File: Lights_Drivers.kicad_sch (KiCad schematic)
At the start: 15 parts, among them Q3 2N7002, Q4 2N7002, Q7 2N7002, U23 SI8261ABC-IS, U24 SI8261ABC-IS, U6 SI8261ABC-IS

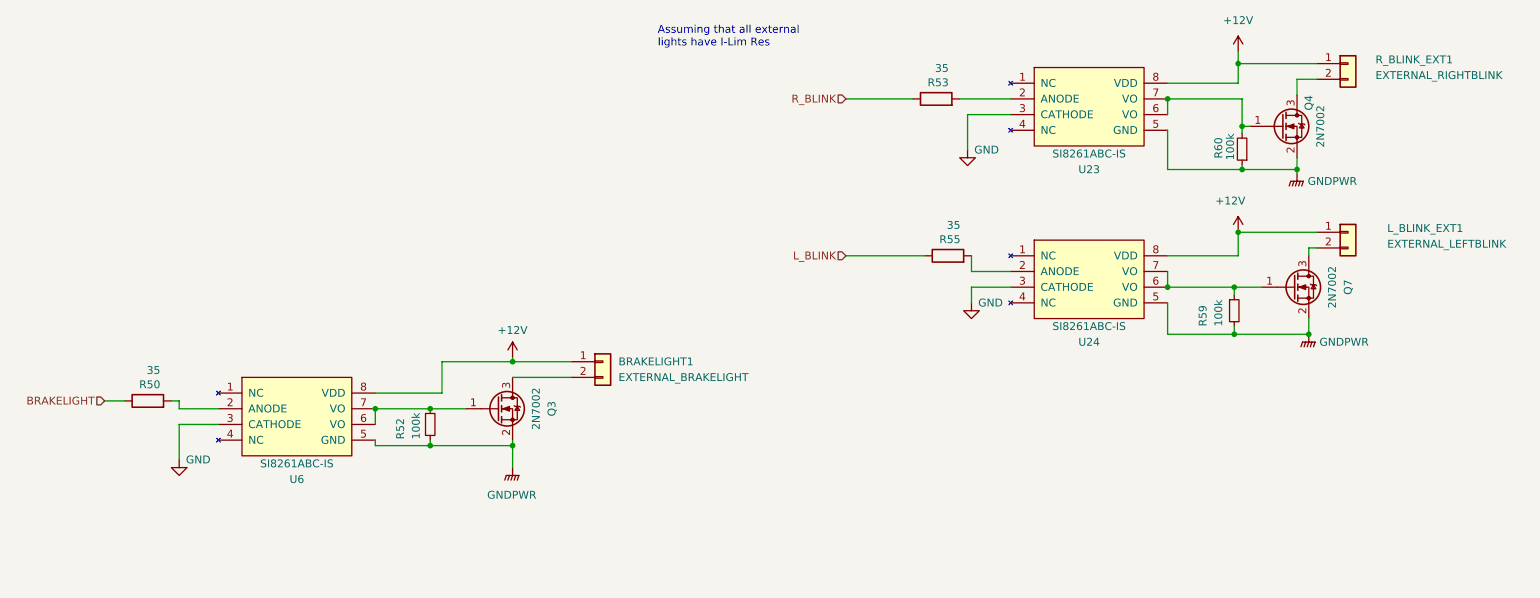
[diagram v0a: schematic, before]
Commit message: Flipped optoisolators, changed resistor values, added second connector to motor can and disconnected shield pins for now since I haven't seen them used (will chack against old version to see what the circuit looked like), copied power-in circuit from contactor board, added optoisolator to timer and blinker light connection.
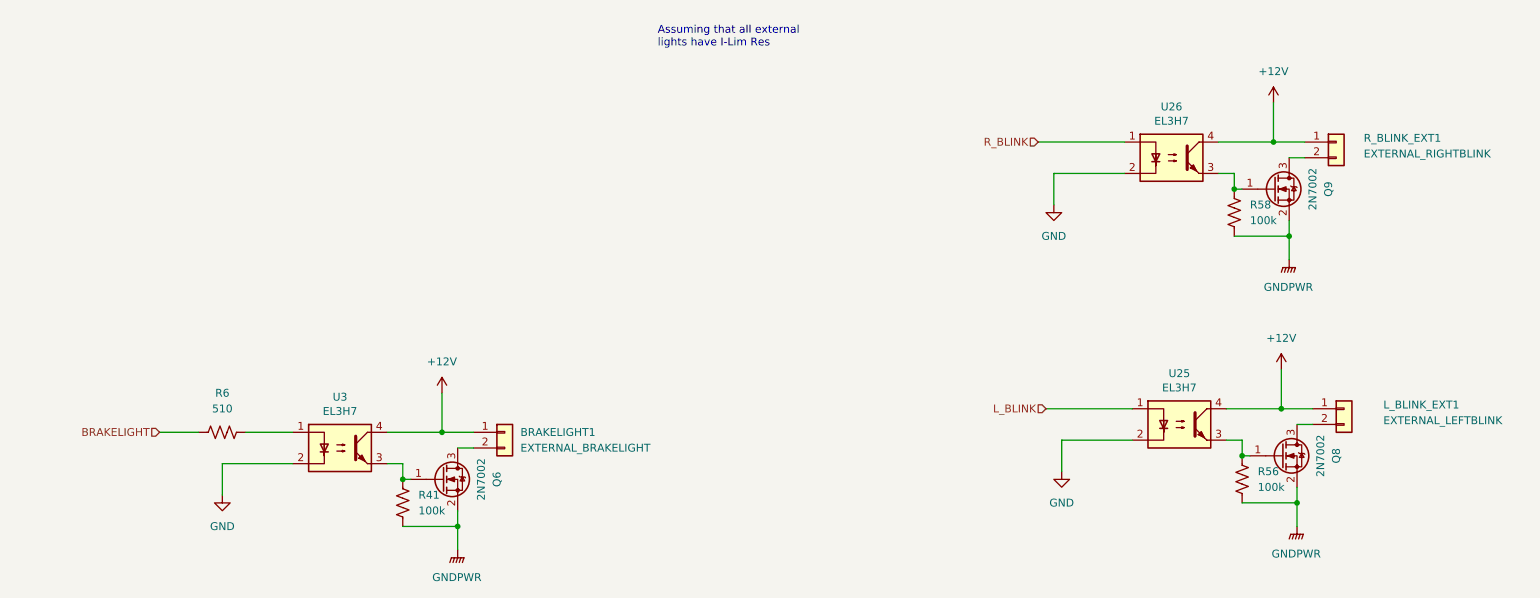
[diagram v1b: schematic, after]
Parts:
- removed Q3, Q4, Q7: 2N7002, Package_TO_SOT_SMD:SOT-23, symbol Transistor_FET:2N7002
- removed R50, R53, R55: 35, Resistor_SMD:R_0805_2012Metric, symbol Device:R
- removed R52, R59, R60: 100k, Resistor_SMD:R_0805_2012Metric, symbol Device:R_Small
- removed U23, U24, U6: SI8261ABC-IS, Package_SO:SOIC-8_3.9x4.9mm_P1.27mm, symbol utsvt-bps:SI8261ABC-IS
- added Q6, Q8, Q9: 2N7002, Package_TO_SOT_SMD:SOT-23, symbol Transistor_FET:2N7002
- added R41, R56, R58: 100k, Resistor_SMD:R_0805_2012Metric, symbol Device:R_US
- added R6: 510, symbol Device:R_US
- added U25, U26, U3: EL3H7, Package_DIP:DIP-4_W7.62mm, symbol Isolator:SFH617A-1
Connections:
- net +12V: now also U25.4, U26.4, U3.4
- net BRAKELIGHT: now also R6.1
- net GND: now also U25.2, U26.2, U3.2
- net GNDPWR: now also Q6.2 (S), Q8.2 (S), Q9.2 (S), R41.2, R56.2, R58.2
- net L_BLINK: now also U25.1
- net R_BLINK: now also U26.1
- net at L_BLINK_EXT1.2 (Pin_2): now also Q8.3 (D)
- net at R_BLINK_EXT1.2 (Pin_2): now also Q9.3 (D)
- net at BRAKELIGHT1.2 (Pin_2): now also Q6.3 (D)
- new net: Q8.1 (G), R56.1, U25.3
- new net: Q9.1 (G), R58.1, U26.3
- new net: Q6.1 (G), R41.1, U3.3
- new net: R6.2, U3.1
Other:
- moved on the sheet: BRAKELIGHT1, L_BLINK_EXT1, R_BLINK_EXT1

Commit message: Added footprints. I think this is everything except the fuse.
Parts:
- R6: footprint (none) -> Resistor_SMD:R_0805_2012Metric
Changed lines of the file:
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@@
 			)
 		)
-		(property "Footprint" ""
+		(property "Footprint" "Resistor_SMD:R_0805_2012Metric"
 			(at 53.594 104.394 90)
 			(effects

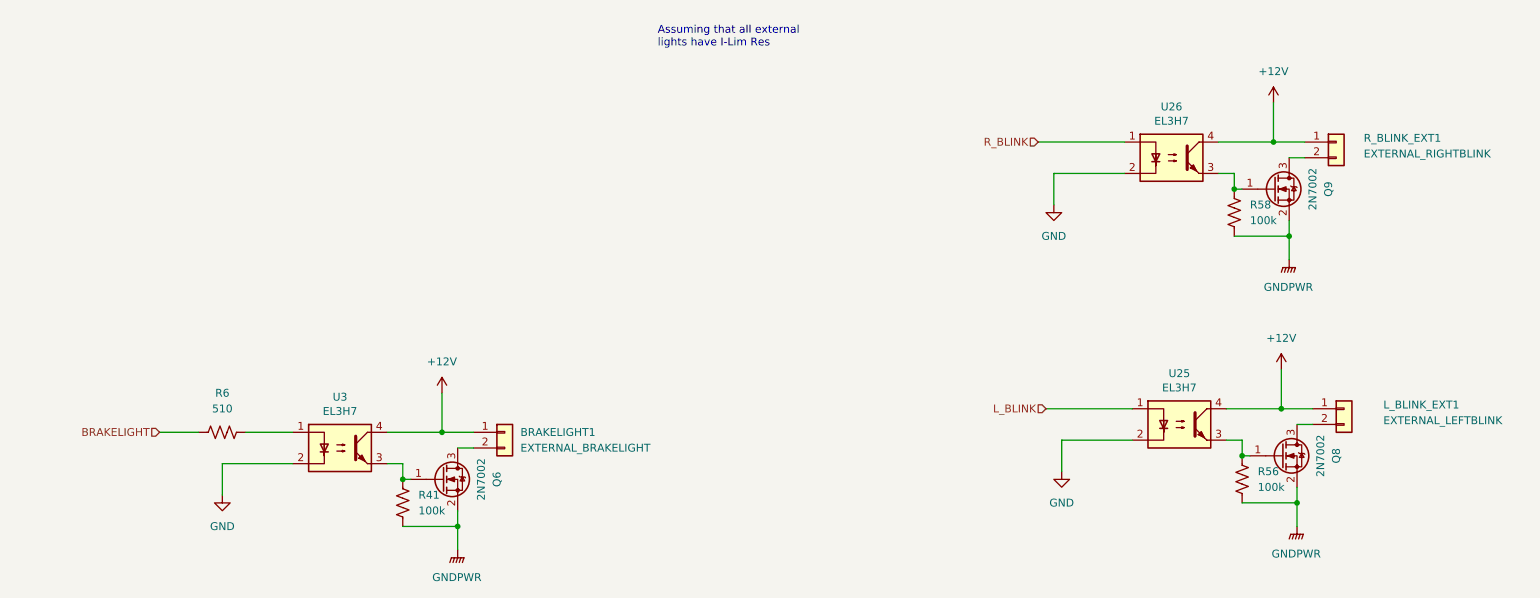
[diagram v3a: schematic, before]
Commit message: renamed power state indicators to contactors and removed unused contactors, added current limiting resistors to lights drivers, changed mosfet to new mosfet
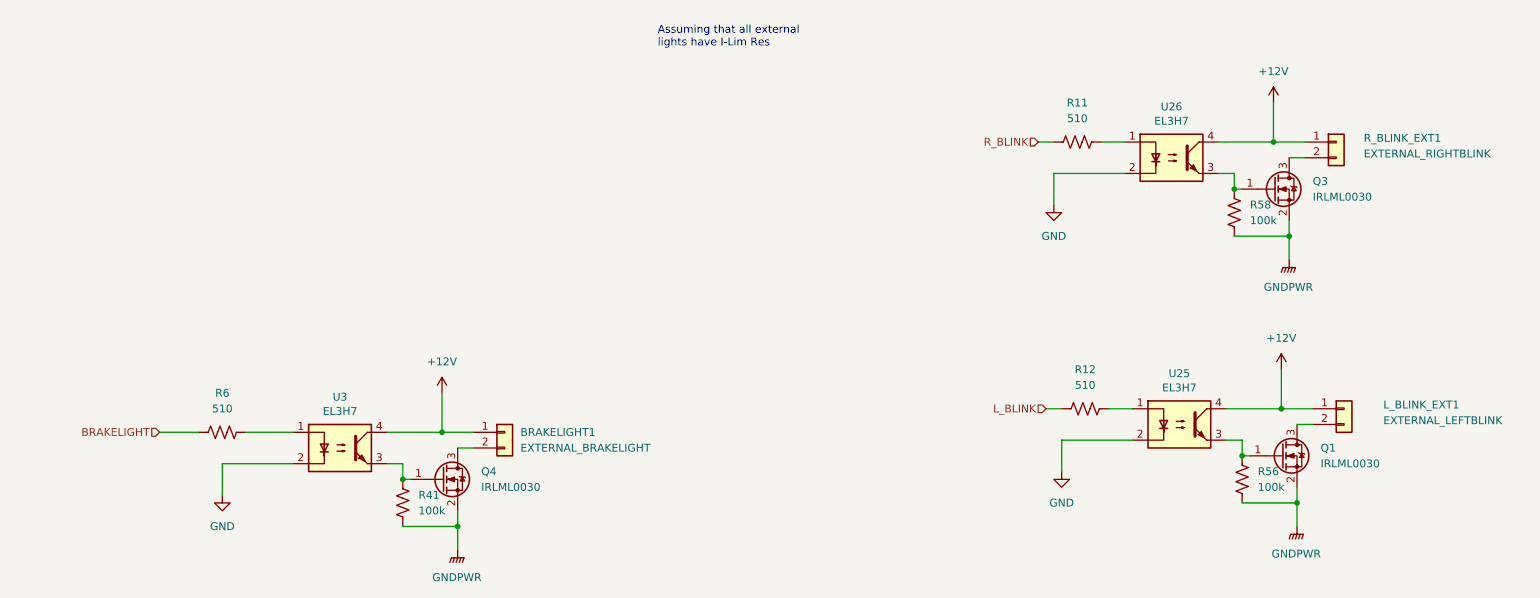
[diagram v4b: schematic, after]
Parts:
- removed Q6, Q8, Q9: 2N7002, Package_TO_SOT_SMD:SOT-23, symbol Transistor_FET:2N7002
- added Q1, Q3, Q4: IRLML0030, Package_TO_SOT_SMD:SOT-23, symbol Transistor_FET:IRLML0030
- added R11, R12: 510, symbol Device:R_US
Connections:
- net GNDPWR: now also Q1.2 (S), Q3.2 (S), Q4.2 (S)
- net L_BLINK: now also R12.1; no longer U25.1
- net R_BLINK: now also R11.1; no longer U26.1
- net at R56.1, U25.3: now also Q1.1 (G)
- net at L_BLINK_EXT1.2 (Pin_2): now also Q1.3 (D)
- net at R58.1, U26.3: now also Q3.1 (G)
- net at R_BLINK_EXT1.2 (Pin_2): now also Q3.3 (D)
- net at R41.1, U3.3: now also Q4.1 (G)
- net at BRAKELIGHT1.2 (Pin_2): now also Q4.3 (D)
- new net: R12.2, U25.1
- new net: R11.2, U26.1

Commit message: fixed some footprints and part numbers
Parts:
- Q1, Q3, Q4: Mouser Part Number (none) -> 771-BUK9M23-80EX
- R11, R12: footprint (none) -> Resistor_SMD:R_0805_2012Metric; Mouser Part Number (none) -> 71-CRCW0805510RFKEAC
- R41, R56, R58: Mouser Part Number (none) -> 71-CRCW0805100KFKEAC
- R6: Mouser Part Number (none) -> 71-CRCW0805510RFKEAC
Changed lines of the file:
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@@
 			)
 		)
-		(property "Footprint" ""
+		(property "Footprint" "Resistor_SMD:R_0805_2012Metric"
 			(at 192.024 57.404 90)
 			(effects
@@
 		)
 		(property "Vds" ""
+			(at 191.77 58.42 0)
+			(effects
+				(font
+					(size 1.27 1.27)
+				)
+				(hide yes)
+			)
+		)
+		(property "Mouser Part Number" "71-CRCW0805510RFKEAC"
 			(at 191.77 58.42 0)
 			(effects
@@
 			)
 		)
+		(property "Mouser Part Number" "771-BUK9M23-80EX"
+			(at 224.79 109.22 0)
+			(effects
+				(font
+					(size 1.27 1.27)
+				)
+				(hide yes)
+			)
+		)
 		(pin "2"
 		)
@@
 			)
 		)
+		(property "Mouser Part Number" "771-BUK9M23-80EX"
+			(at 223.52 66.04 0)
+			(effects
+				(font
+					(size 1.27 1.27)
+				)
+				(hide yes)
+			)
+		)
 		(pin "2"
 		)
@@
 			)
 		)
-		(property "Footprint" ""
+		(property "Footprint" "Resistor_SMD:R_0805_2012Metric"
 			(at 193.294 100.584 90)
 			(effects
@@
 		)
 		(property "Vds" ""
+			(at 193.04 101.6 0)
+			(effects
+				(font
+					(size 1.27 1.27)
+				)
+				(hide yes)
+			)
+		)
+		(property "Mouser Part Number" "71-CRCW0805510RFKEAC"
 			(at 193.04 101.6 0)
 			(effects
@@
 			)
 		)
+		(property "Mouser Part Number" "71-CRCW0805100KFKEAC"
+			(at 82.55 116.84 0)
+			(effects
+				(font
+					(size 1.27 1.27)
+				)
+				(hide yes)
+			)
+		)
 		(pin "2"
 		)
@@
 			)
 		)
+		(property "Mouser Part Number" "771-BUK9M23-80EX"
+			(at 88.9 113.03 0)
+			(effects
+				(font
+					(size 1.27 1.27)
+				)
+				(hide yes)
+			)
+		)
 		(pin "2"
 		)
@@
 			)
 		)
+		(property "Mouser Part Number" "71-CRCW0805100KFKEAC"
+			(at 218.44 113.03 0)
+			(effects
+				(font
+					(size 1.27 1.27)
+				)
+				(hide yes)
+			)
+		)
 		(pin "2"
 		)
@@
 			)
 		)
+		(property "Mouser Part Number" "71-CRCW0805510RFKEAC"
+			(at 53.34 105.41 0)
+			(effects
+				(font
+					(size 1.27 1.27)
+				)
+				(hide yes)
+			)
+		)
 		(pin "2"
 		)
@@
 			(at 217.17 69.85 0)
 			(effects
+				(font
+					(size 1.27 1.27)
+				)
+				(hide yes)
+			)
+		)
+		(property "Mouser Part Number" "71-CRCW0805100KFKEAC"
+			(at 217.17 69.85 0)
+			(effects

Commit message: Added/checked datasheet links/part numbers, deleted accel_pot2 and brake_pot2 hierarchical labels and changed corresponding pins (PC2, PC3) to GPIO on the now-2x5 extra GPIO connector.
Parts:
- Q1, Q3, Q4: Mouser Part Number 771-BUK9M23-80EX -> (none); P/N (none) -> IRLML0030TRPBF
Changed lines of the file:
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@@
 			)
 		)
-		(property "Datasheet" "https://everlightamericas.com/index.php?controller=attachment&id_attachment=2584"
+		(property "Datasheet" "https://www.mouser.com/ProductDetail/Everlight/EL3H7DTA-VG?qs=8PzhAHr7IdO5ivSzPAFioA%3D%3D&utm_id=21629221803&gad_source=1&gclid=Cj0KCQiArby5BhCDARIsAIJvjIRxO0jcjcKfnV1hER0ZGDMF9W_FecGmdKXwVqQCsmJYIZvEtRfuUkAaAnFwEALw_wcB"
 			(at 208.28 104.14 0)
 			(effects
@@
 			)
 		)
-		(property "Datasheet" "~"
+		(property "Datasheet" "https://www.mouser.in/ProductDetail/Vishay-Dale/CRCW0805510RFKEAC?qs=E3Y5ESvWgWP%252BBvcXzqF1aQ%3D%3D"
 			(at 191.77 58.42 0)
 			(effects
@@
 			)
 		)
-		(property "Mouser Part Number" "771-BUK9M23-80EX"
+		(property "Mouser Part Number" ""
+			(at 224.79 109.22 0)
+			(effects
+				(font
+					(size 1.27 1.27)
+				)
+				(hide yes)
+			)
+		)
+		(property "P/N" "  IRLML0030TRPBF"
 			(at 224.79 109.22 0)
 			(effects
@@
 			)
 		)
-		(property "Datasheet" "https://everlightamericas.com/index.php?controller=attachment&id_attachment=2584"
+		(property "Datasheet" "https://www.mouser.com/ProductDetail/Everlight/EL3H7DTA-VG?qs=8PzhAHr7IdO5ivSzPAFioA%3D%3D&utm_id=21629221803&gad_source=1&gclid=Cj0KCQiArby5BhCDARIsAIJvjIRxO0jcjcKfnV1hER0ZGDMF9W_FecGmdKXwVqQCsmJYIZvEtRfuUkAaAnFwEALw_wcB"
 			(at 72.39 107.95 0)
 			(effects
@@
 			)
 		)
-		(property "Mouser Part Number" "771-BUK9M23-80EX"
+		(property "Mouser Part Number" ""
+			(at 223.52 66.04 0)
+			(effects
+				(font
+					(size 1.27 1.27)
+				)
+				(hide yes)
+			)
+		)
+		(property "P/N" "  IRLML0030TRPBF"
 			(at 223.52 66.04 0)
 			(effects
@@
 			)
 		)
-		(property "Datasheet" "~"
+		(property "Datasheet" "https://www.mouser.in/ProductDetail/Vishay-Dale/CRCW0805510RFKEAC?qs=E3Y5ESvWgWP%252BBvcXzqF1aQ%3D%3D"
 			(at 193.04 101.6 0)
 			(effects
@@
 			)
 		)
-		(property "Datasheet" "~"
+		(property "Datasheet" "https://www.mouser.in/ProductDetail/Vishay-Dale/CRCW0805100KFKEAC?qs=E3Y5ESvWgWORJvbAiaO1ug%3D%3D"
 			(at 82.55 116.84 0)
 			(effects
@@
 			)
 		)
-		(property "Datasheet" "https://everlightamericas.com/index.php?controller=attachment&id_attachment=2584"
+		(property "Datasheet" "https://www.mouser.com/ProductDetail/Everlight/EL3H7DTA-VG?qs=8PzhAHr7IdO5ivSzPAFioA%3D%3D&utm_id=21629221803&gad_source=1&gclid=Cj0KCQiArby5BhCDARIsAIJvjIRxO0jcjcKfnV1hER0ZGDMF9W_FecGmdKXwVqQCsmJYIZvEtRfuUkAaAnFwEALw_wcB"
 			(at 207.01 60.96 0)
 			(effects
@@
 			)
 		)
-		(property "Mouser Part Number" "771-BUK9M23-80EX"
+		(property "Mouser Part Number" ""
+			(at 88.9 113.03 0)
+			(effects
+				(font
+					(size 1.27 1.27)
+				)
+				(hide yes)
+			)
+		)
+		(property "P/N" "  IRLML0030TRPBF"
 			(at 88.9 113.03 0)
 			(effects
@@
 			)
 		)
-		(property "Datasheet" "~"
+		(property "Datasheet" "https://www.mouser.in/ProductDetail/Vishay-Dale/CRCW0805100KFKEAC?qs=E3Y5ESvWgWORJvbAiaO1ug%3D%3D"
 			(at 218.44 113.03 0)
 			(effects
@@
 			)
 		)
-		(property "Datasheet" "~"
+		(property "Datasheet" "https://www.mouser.in/ProductDetail/Vishay-Dale/CRCW0805510RFKEAC?qs=E3Y5ESvWgWP%252BBvcXzqF1aQ%3D%3D"
 			(at 53.34 105.41 0)
 			(effects
@@
 			)
 		)
-		(property "Datasheet" "~"
+		(property "Datasheet" "https://www.mouser.in/ProductDetail/Vishay-Dale/CRCW0805100KFKEAC?qs=E3Y5ESvWgWORJvbAiaO1ug%3D%3D"
 			(at 217.17 69.85 0)
 			(effects

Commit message: Changed EL3H7 footprint from through-hole to SMD.
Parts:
- U25, U26, U3: footprint Package_DIP:DIP-4_W7.62mm -> Package_SO:SSOP-4_4.4x2.6mm_P1.27mm
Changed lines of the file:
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@@
 			)
 		)
-		(property "Footprint" "Package_DIP:DIP-4_W7.62mm"
+		(property "Footprint" "Package_SO:SSOP-4_4.4x2.6mm_P1.27mm"
 			(at 203.2 109.22 0)
 			(effects
@@
 			)
 		)
-		(property "Footprint" "Package_DIP:DIP-4_W7.62mm"
+		(property "Footprint" "Package_SO:SSOP-4_4.4x2.6mm_P1.27mm"
 			(at 67.31 113.03 0)
 			(effects
@@
 			)
 		)
-		(property "Footprint" "Package_DIP:DIP-4_W7.62mm"
+		(property "Footprint" "Package_SO:SSOP-4_4.4x2.6mm_P1.27mm"
 			(at 201.93 66.04 0)
 			(effects

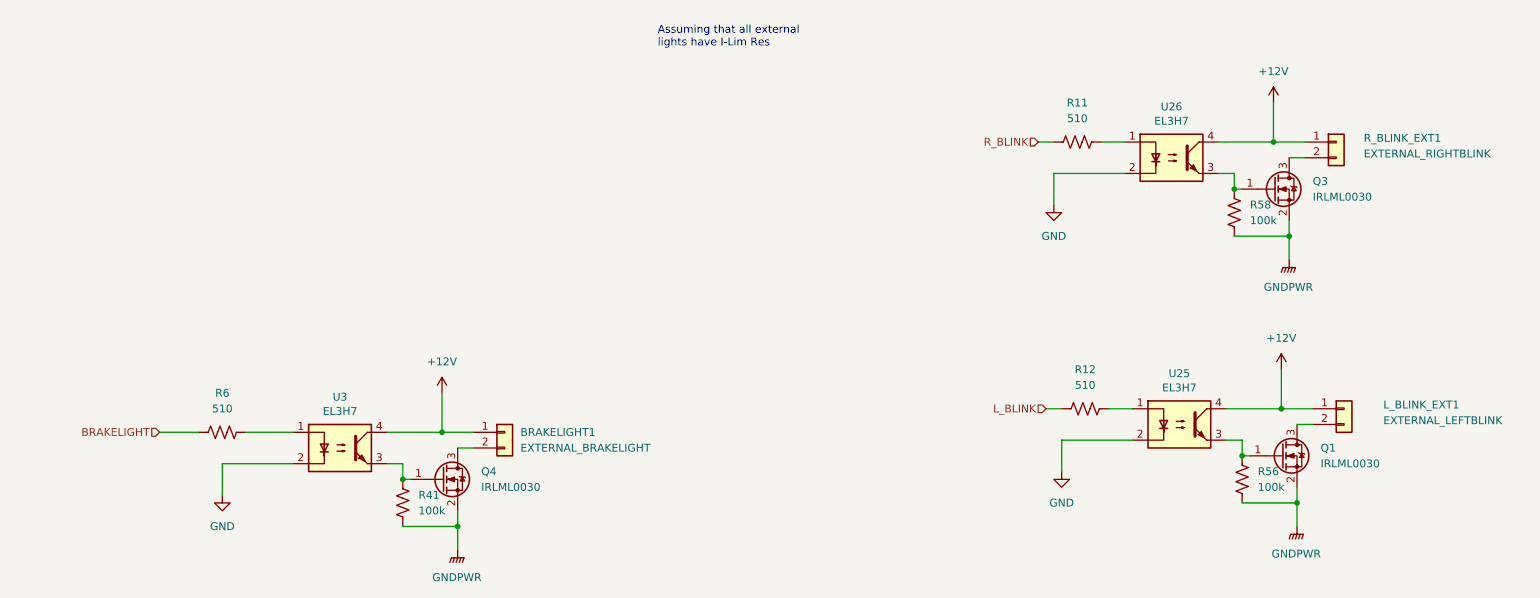
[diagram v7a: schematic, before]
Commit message: Added 3A fuse to lights (estimated 9 lights, ~1.8 A plus buffer, changed fuse datasheet to match part number.
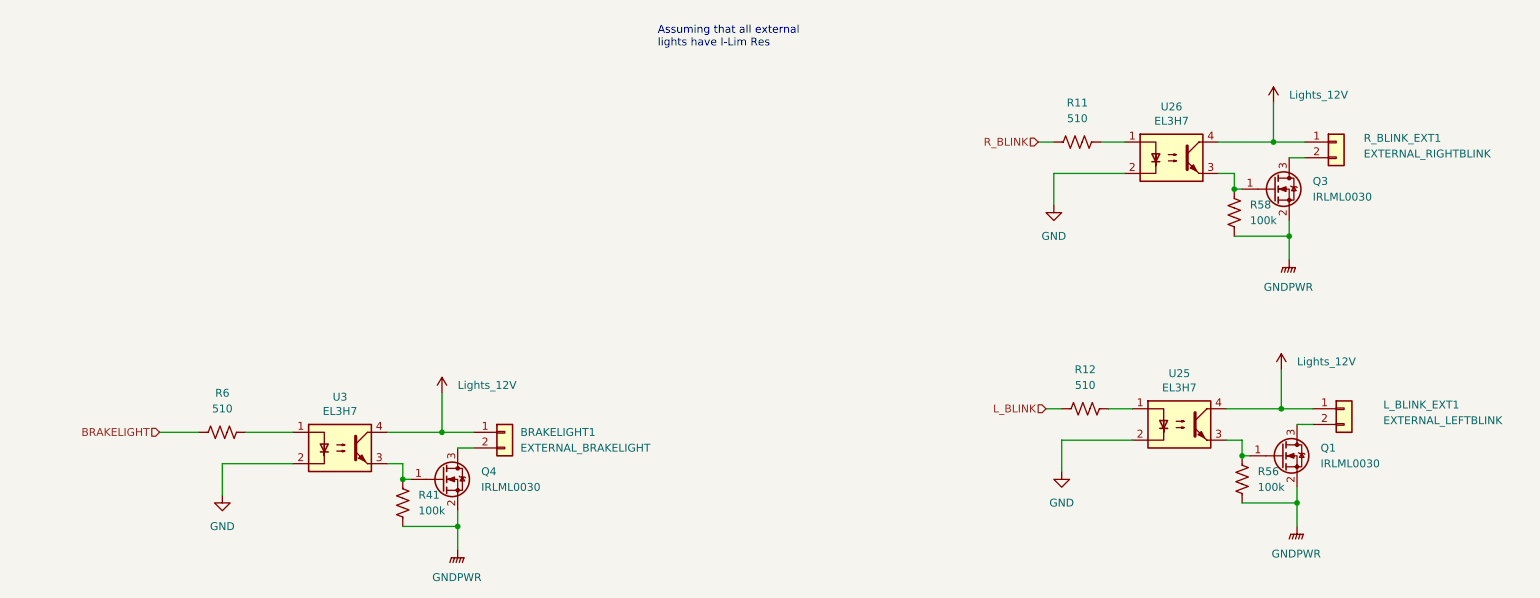
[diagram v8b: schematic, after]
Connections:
- net +12V renamed Lights_12V
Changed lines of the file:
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@@
 			)
 		)
-		(property "Value" "+12V"
-			(at 223.52 46.99 0)
-			(effects
-				(font
-					(size 1.27 1.27)
-				)
+		(property "Value" "Lights_12V"
+			(at 226.06 50.7999 0)
+			(effects
+				(font
+					(size 1.27 1.27)
+				)
+				(justify left)
 			)
 		)
@@
 			)
 		)
-		(property "Value" "+12V"
-			(at 88.9 93.98 0)
-			(effects
-				(font
-					(size 1.27 1.27)
-				)
+		(property "Value" "Lights_12V"
+			(at 91.44 97.7899 0)
+			(effects
+				(font
+					(size 1.27 1.27)
+				)
+				(justify left)
 			)
 		)
@@
 			)
 		)
-		(property "Value" "+12V"
-			(at 224.79 90.17 0)
-			(effects
-				(font
-					(size 1.27 1.27)
-				)
-			)
-		)
+		(property "Value" "Lights_12V"
+			(at 227.33 93.9799 0)
+			(effects
+				(font
+					(size 1.27 1.27)
+				)
+				(justify left)
+			)
+		)
